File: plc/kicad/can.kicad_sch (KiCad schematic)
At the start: 7 parts, among them CN10 DB2ERC-5.08-4P, SW4 MSK12C02, U14 TCAN337DR

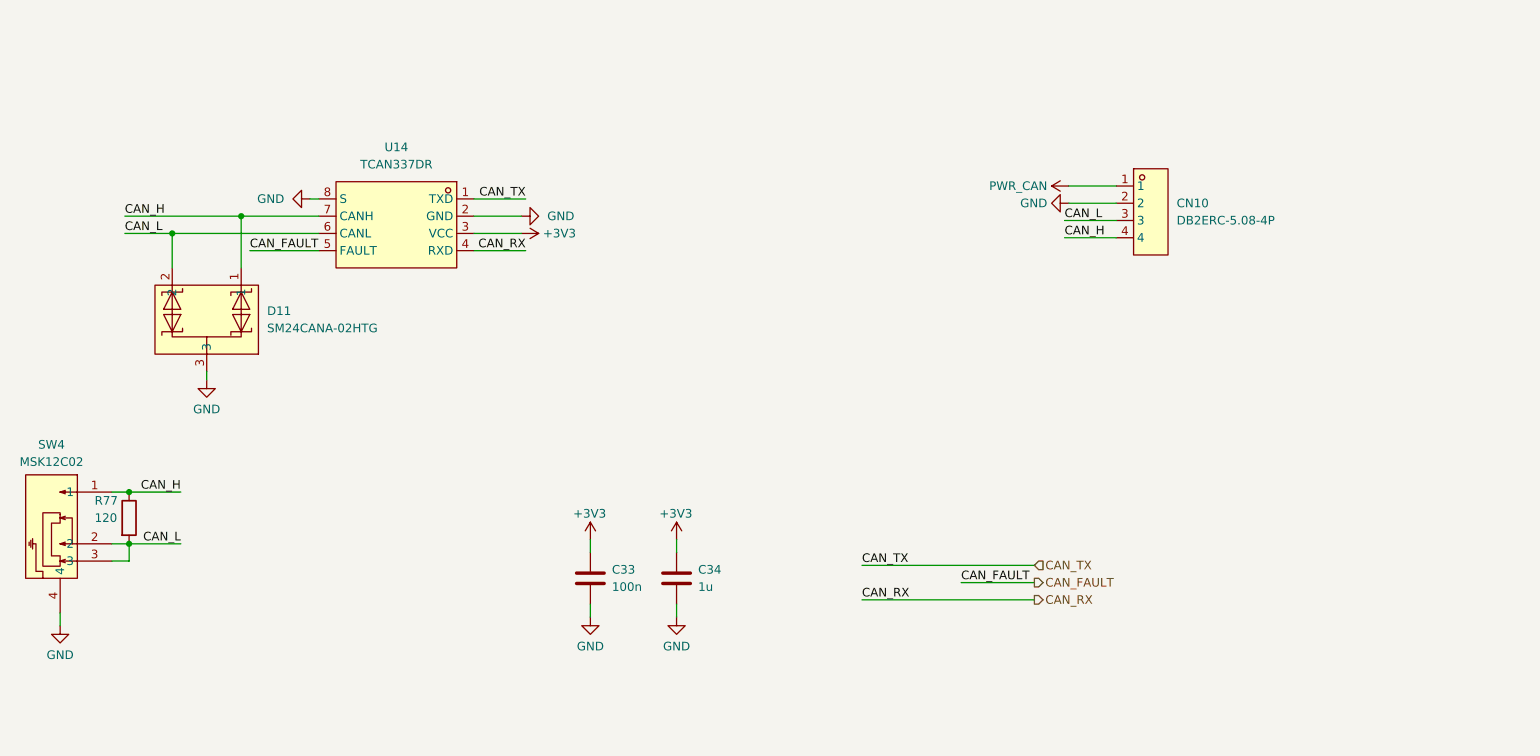
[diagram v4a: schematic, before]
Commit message: AHT20 sensor added
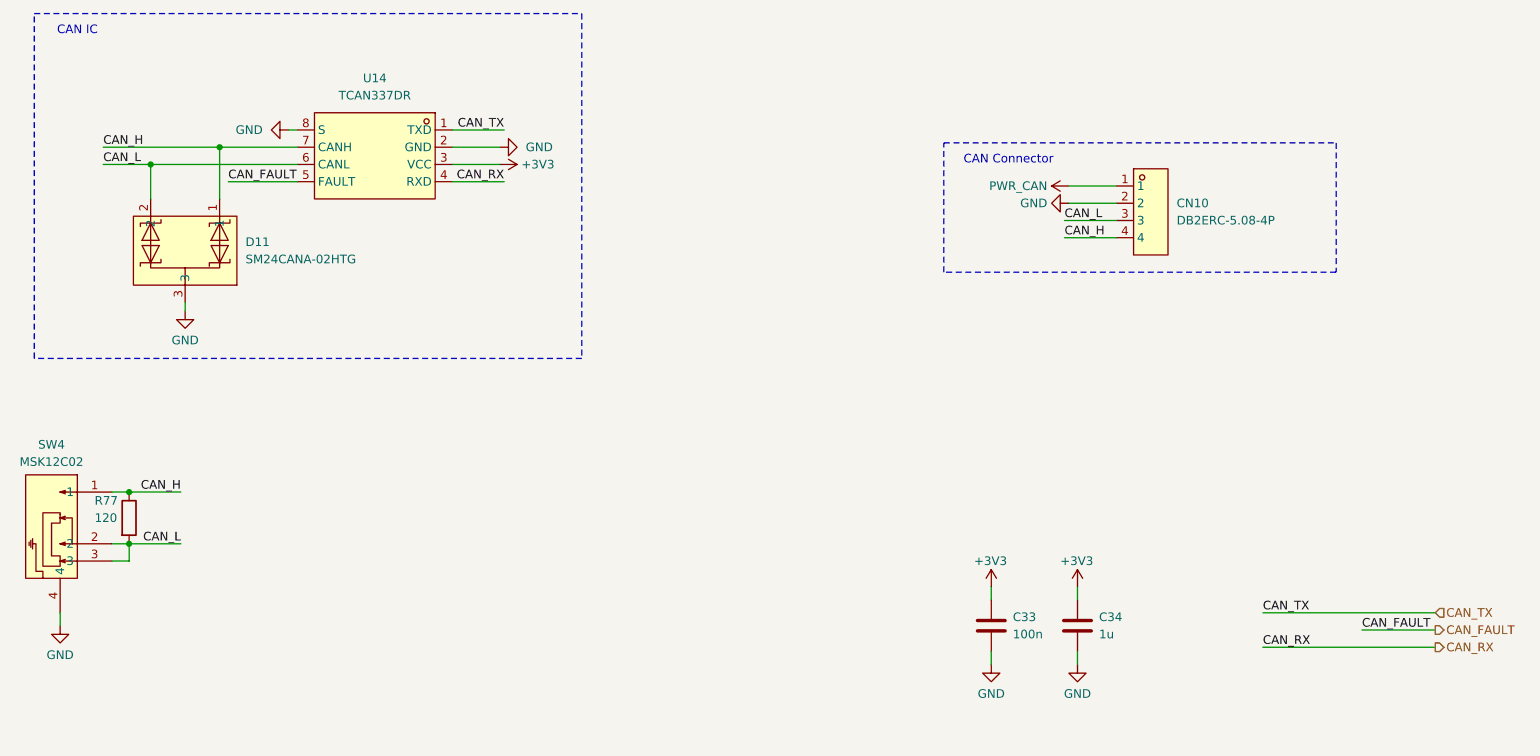
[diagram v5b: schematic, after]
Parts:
- C33, C34: footprint Capacitor_SMD:C_0805_2012Metric -> Capacitor_SMD:C_0603_1608Metric
- R77: footprint Resistor_SMD:R_0805_2012Metric -> Resistor_SMD:R_0603_1608Metric
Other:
- note added: "CAN Connector"
- note added: "CAN IC"
- moved on the sheet: C33, C34, D11, U14

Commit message: PCB placement
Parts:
- renumbered C33 to C40, C34 to C41, CN10 to CN11, D11 to D15, R77 to R80, U14 to U18
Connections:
- net CAN_H: now also CN11.3; no longer CN11.4
- net CAN_L: now also CN11.4; no longer CN11.3
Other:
- title: (none) -> LibrePLC32
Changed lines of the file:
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@@
 	(generator_version "10.0")
 	(paper "A4")
+	(title_block
+		(title "LibrePLC32")
+		(date "2026-04-12")
+		(rev "A")
+	)
 	(rectangle
 		(start 39.37 59.055)
@@
 		)
 	)
+	(label "CAN_H"
+		(at 191.135 89.535 0)
+		(effects
+			(font
+				(size 1.27 1.27)
+			)
+			(justify left bottom)
+		)
+	)
 	(label "CAN_TX"
 		(at 108.585 76.2 180)
@@
 	)
 	(label "CAN_L"
-		(at 191.135 89.535 0)
-		(effects
-			(font
-				(size 1.27 1.27)
-			)
-			(justify left bottom)
-		)
-	)
-	(label "CAN_L"
 		(at 60.96 137.16 180)
 		(effects
@@
 	)
 	(label "CAN_H"
+		(at 60.96 129.54 180)
+		(effects
+			(font
+				(size 1.27 1.27)
+			)
+			(justify right bottom)
+		)
+	)
+	(label "CAN_L"
 		(at 191.135 92.075 0)
 		(effects
@@
 			)
 			(justify left bottom)
-		)
-	)
-	(label "CAN_H"
-		(at 60.96 129.54 180)
-		(effects
-			(font
-				(size 1.27 1.27)
-			)
-			(justify right bottom)
 		)
 	)
@@
 		(in_pos_files yes)
 		(dnp no)
-		(property "Reference" "#PWR0160"
+		(property "Reference" "#PWR0199"
 			(at 193.04 147.32 0)
 			(hide yes)
@@
 			(project "LibrePLC32"
 				(path "/ef4c1a27-85a3-413a-9f93-a41c4f97eee5/1f15b1b2-5031-4e14-8391-148d71dbf666"
-					(reference "#PWR0160")
+					(reference "#PWR0199")
 					(unit 1)
 				)
@@
 		(dnp no)
 		(fields_autoplaced yes)
-		(property "Reference" "#PWR0161"
+		(property "Reference" "#PWR0200"
 			(at 193.04 161.29 0)
 			(hide yes)
@@
 			(project "LibrePLC32"
 				(path "/ef4c1a27-85a3-413a-9f93-a41c4f97eee5/1f15b1b2-5031-4e14-8391-148d71dbf666"
-					(reference "#PWR0161")
+					(reference "#PWR0200")
 					(unit 1)
 				)
@@
 		(in_pos_files yes)
 		(dnp no)
-		(property "Reference" "#PWR0155"
+		(property "Reference" "#PWR0192"
 			(at 70.485 76.2 0)
 			(hide yes)
@@
 			(project "LibrePLC32"
 				(path "/ef4c1a27-85a3-413a-9f93-a41c4f97eee5/1f15b1b2-5031-4e14-8391-148d71dbf666"
-					(reference "#PWR0155")
+					(reference "#PWR0192")
 					(unit 1)
 				)
@@
 		(dnp no)
 		(fields_autoplaced yes)
-		(property "Reference" "#PWR0153"
+		(property "Reference" "#PWR0190"
 			(at 43.18 155.575 0)
 			(hide yes)
@@
 			(project "LibrePLC32"
 				(path "/ef4c1a27-85a3-413a-9f93-a41c4f97eee5/1f15b1b2-5031-4e14-8391-148d71dbf666"
-					(reference "#PWR0153")
+					(reference "#PWR0190")
 					(unit 1)
 				)
@@
 		(dnp no)
 		(fields_autoplaced yes)
-		(property "Reference" "D11"
+		(property "Reference" "D15"
 			(at 70.485 92.7099 0)
 			(show_name no)
@@
 			(project "LibrePLC32"
 				(path "/ef4c1a27-85a3-413a-9f93-a41c4f97eee5/1f15b1b2-5031-4e14-8391-148d71dbf666"
-					(reference "D11")
+					(reference "D15")
 					(unit 1)
 				)
@@
 		(in_pos_files yes)
 		(dnp no)
-		(property "Reference" "#PWR0157"
+		(property "Reference" "#PWR0194"
 			(at 104.14 81.28 0)
 			(hide yes)
@@
 			(project "LibrePLC32"
 				(path "/ef4c1a27-85a3-413a-9f93-a41c4f97eee5/1f15b1b2-5031-4e14-8391-148d71dbf666"
-					(reference "#PWR0157")
+					(reference "#PWR0194")
 					(unit 1)
 				)
@@
 		(dnp no)
 		(fields_autoplaced yes)
-		(property "Reference" "C33"
+		(property "Reference" "C40"
 			(at 183.515 147.9549 0)
 			(show_name no)
@@
 			(project "LibrePLC32"
 				(path "/ef4c1a27-85a3-413a-9f93-a41c4f97eee5/1f15b1b2-5031-4e14-8391-148d71dbf666"
-					(reference "C33")
+					(reference "C40")
 					(unit 1)
 				)
@@
 		(in_pos_files yes)
 		(dnp no)
-		(property "Reference" "#PWR0156"
+		(property "Reference" "#PWR0193"
 			(at 114.3 78.74 0)
 			(hide yes)
@@
 			(project "LibrePLC32"
 				(path "/ef4c1a27-85a3-413a-9f93-a41c4f97eee5/1f15b1b2-5031-4e14-8391-148d71dbf666"
-					(reference "#PWR0156")
+					(reference "#PWR0193")
 					(unit 1)
 				)
@@
 		(in_pos_files yes)
 		(dnp no)
-		(property "Reference" "R77"
+		(property "Reference" "R80"
 			(at 48.26 130.81 0)
 			(show_name no)
@@
 			(project "LibrePLC32"
 				(path "/ef4c1a27-85a3-413a-9f93-a41c4f97eee5/1f15b1b2-5031-4e14-8391-148d71dbf666"
-					(reference "R77")
+					(reference "R80")
 					(unit 1)
 				)
@@
 		(dnp no)
 		(fields_autoplaced yes)
-		(property "Reference" "C34"
+		(property "Reference" "C41"
 			(at 196.215 147.9549 0)
 			(show_name no)
@@
 			(project "LibrePLC32"
 				(path "/ef4c1a27-85a3-413a-9f93-a41c4f97eee5/1f15b1b2-5031-4e14-8391-148d71dbf666"
-					(reference "C34")
+					(reference "C41")
 					(unit 1)
 				)
@@
 		(dnp no)
 		(fields_autoplaced yes)
-		(property "Reference" "#PWR0163"
+		(property "Reference" "#PWR0198"
 			(at 185.42 86.995 0)
 			(hide yes)
@@
 			(project "LibrePLC32"
 				(path "/ef4c1a27-85a3-413a-9f93-a41c4f97eee5/1f15b1b2-5031-4e14-8391-148d71dbf666"
-					(reference "#PWR0163")
+					(reference "#PWR0198")
 					(unit 1)
 				)
@@
 		(dnp no)
 		(fields_autoplaced yes)
-		(property "Reference" "#PWR0159"
+		(property "Reference" "#PWR0196"
 			(at 180.34 161.29 0)
 			(hide yes)
@@
 			(project "LibrePLC32"
 				(path "/ef4c1a27-85a3-413a-9f93-a41c4f97eee5/1f15b1b2-5031-4e14-8391-148d71dbf666"
-					(reference "#PWR0159")
+					(reference "#PWR0196")
 					(unit 1)
 				)
@@
 		(in_pos_files yes)
 		(dnp no)
-		(property "Reference" "U14"
+		(property "Reference" "U18"
 			(at 89.535 68.58 0)
 			(show_name no)
@@
 			(project "LibrePLC32"
 				(path "/ef4c1a27-85a3-413a-9f93-a41c4f97eee5/1f15b1b2-5031-4e14-8391-148d71dbf666"
-					(reference "U14")
+					(reference "U18")
 					(unit 1)
 				)
@@
 		(dnp no)
 		(fields_autoplaced yes)
-		(property "Reference" "#PWR0162"
+		(property "Reference" "#PWR0197"
 			(at 195.58 84.455 0)
 			(hide yes)
@@
 			(project "LibrePLC32"
 				(path "/ef4c1a27-85a3-413a-9f93-a41c4f97eee5/1f15b1b2-5031-4e14-8391-148d71dbf666"
-					(reference "#PWR0162")
+					(reference "#PWR0197")
 					(unit 1)
 				)
@@
 		(dnp no)
 		(fields_autoplaced yes)
-		(property "Reference" "#PWR0154"
+		(property "Reference" "#PWR0191"
 			(at 61.595 109.22 0)
 			(hide yes)
@@
 			(project "LibrePLC32"
 				(path "/ef4c1a27-85a3-413a-9f93-a41c4f97eee5/1f15b1b2-5031-4e14-8391-148d71dbf666"
-					(reference "#PWR0154")
+					(reference "#PWR0191")
 					(unit 1)
 				)
@@
 		(dnp no)
 		(fields_autoplaced yes)
-		(property "Reference" "CN10"
+		(property "Reference" "CN11"
 			(at 207.645 86.9949 0)
 			(show_name no)
@@
 			(project "LibrePLC32"
 				(path "/ef4c1a27-85a3-413a-9f93-a41c4f97eee5/1f15b1b2-5031-4e14-8391-148d71dbf666"
-					(reference "CN10")
+					(reference "CN11")
 					(unit 1)
 				)
@@
 		(in_pos_files yes)
 		(dnp no)
-		(property "Reference" "#PWR0158"
+		(property "Reference" "#PWR0195"
 			(at 180.34 147.32 0)
 			(hide yes)
@@
 			(project "LibrePLC32"
 				(path "/ef4c1a27-85a3-413a-9f93-a41c4f97eee5/1f15b1b2-5031-4e14-8391-148d71dbf666"
-					(reference "#PWR0158")
+					(reference "#PWR0195")
 					(unit 1)
 				)

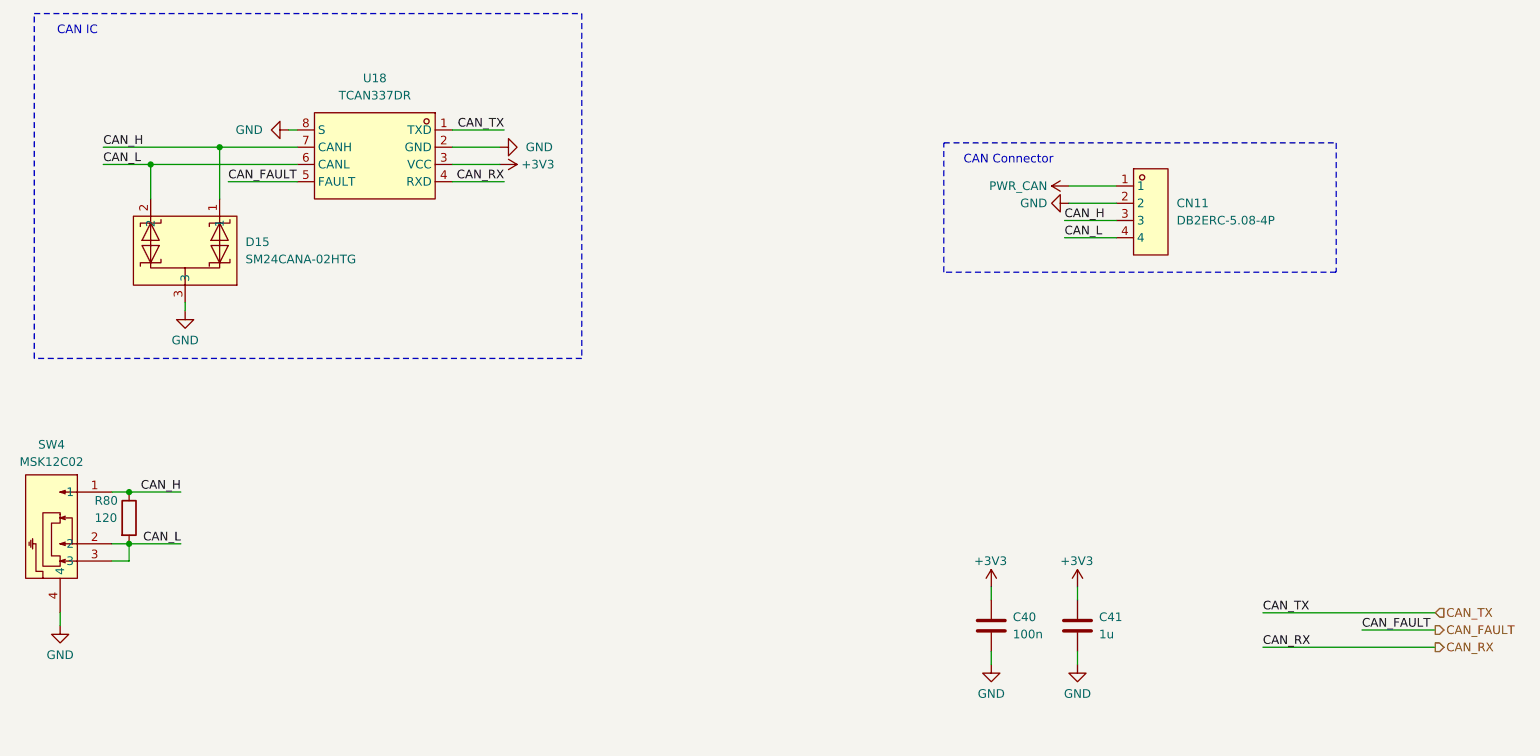
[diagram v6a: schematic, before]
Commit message: Revised CAN circuit
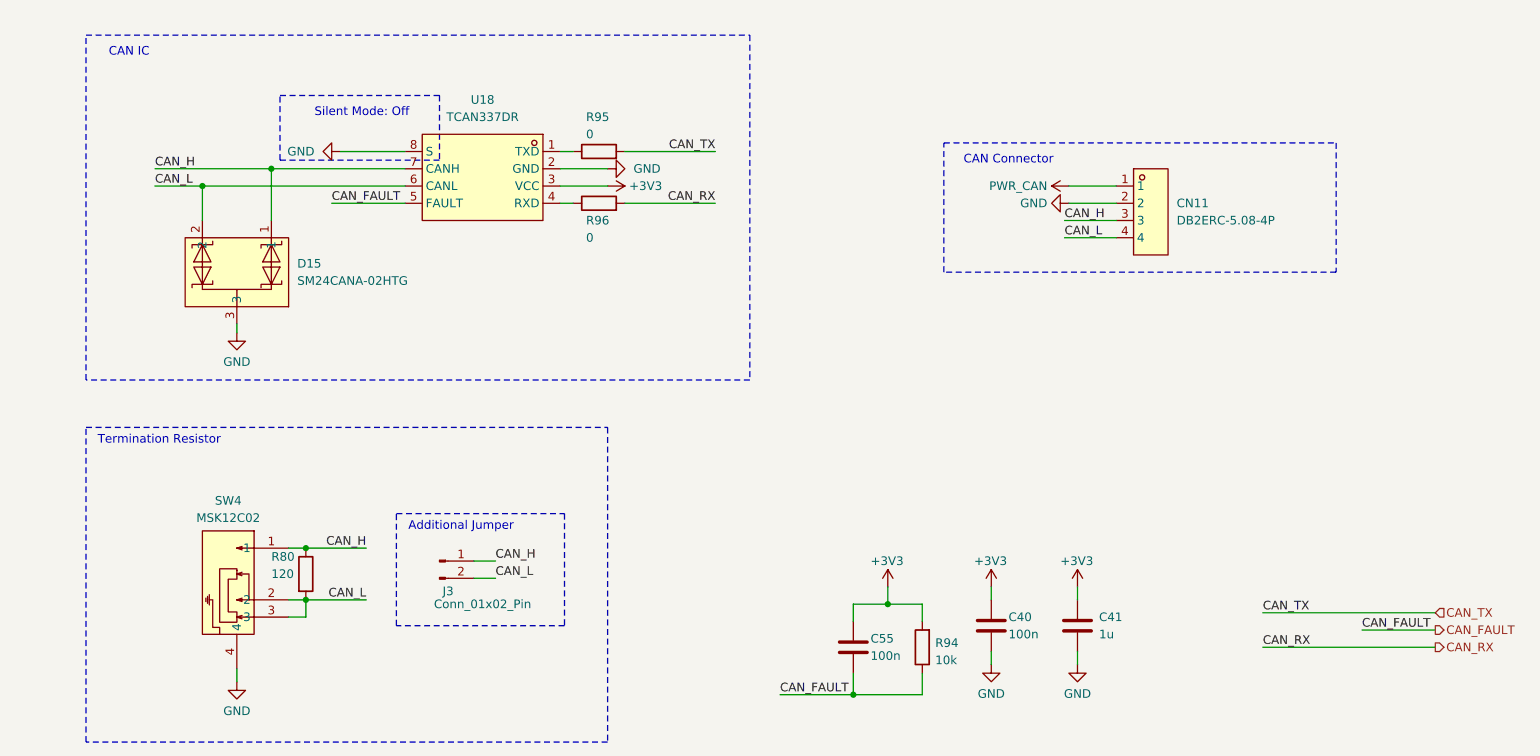
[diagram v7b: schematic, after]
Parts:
- added C55: 100n, Capacitor_SMD:C_0603_1608Metric, symbol Device:C
- added J3: Conn_01x02_Pin, Connector_PinSocket_2.54mm:PinSocket_1x02_P2.54mm_Vertical, symbol Connector:Conn_01x02_Pin
- added R94: 10k, Resistor_SMD:R_0603_1608Metric, symbol Device:R
- added R95, R96: 0, Resistor_SMD:R_0603_1608Metric, symbol Device:R
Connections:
- net +3V3: now also C55.1, R94.2
- net CAN_FAULT: now also C55.2, R94.1
- net CAN_H: now also J3.1 (Pin_1)
- net CAN_L: now also J3.2 (Pin_2)
- net CAN_RX: now also R96.2; no longer U18.4 (RXD)
- net CAN_TX: now also R95.2; no longer U18.1 (TXD)
- new net: R95.1, U18.1 (TXD)
- new net: R96.1, U18.4 (RXD)
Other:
- note added: "Additional Jumper"
- note added: "Silent Mode: Off"
- note added: "Termination Resistor"
- moved on the sheet: D15, R80, SW4, U18
